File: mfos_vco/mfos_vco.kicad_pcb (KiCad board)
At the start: 2 copper layers, 137.2 x 76.2 mm, 117 parts, among them J1 Conn_01x08_Pin, J2 Conn_01x03_Pin, J3 Conn_01x01_Pin, J4 Conn_01x04_Pin, J5 Conn_01x03_Pin, J6 Conn_01x01_Pin, J7 Conn_01x01_Pin, J8 Conn_01x02_Pin, Q1 PN4391, Q1Ar1 2N3904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

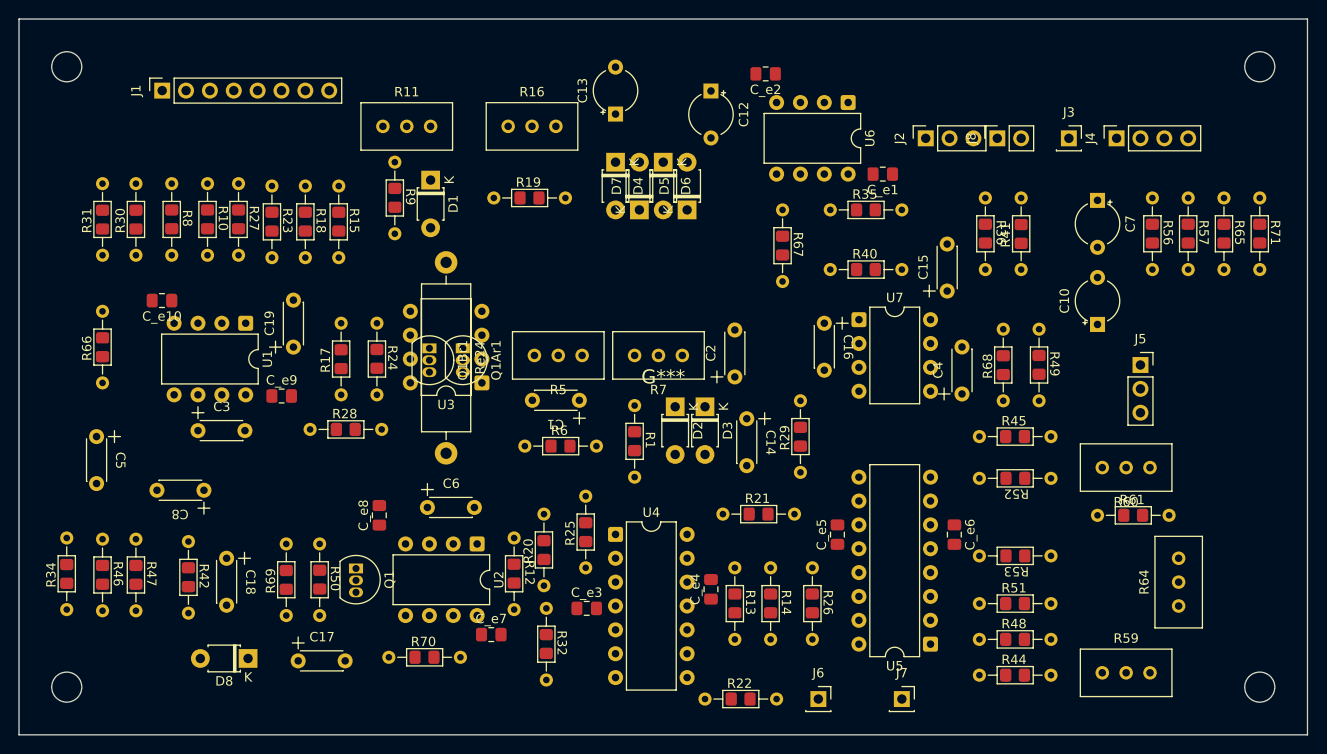
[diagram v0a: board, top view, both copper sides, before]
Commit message: first partial routing
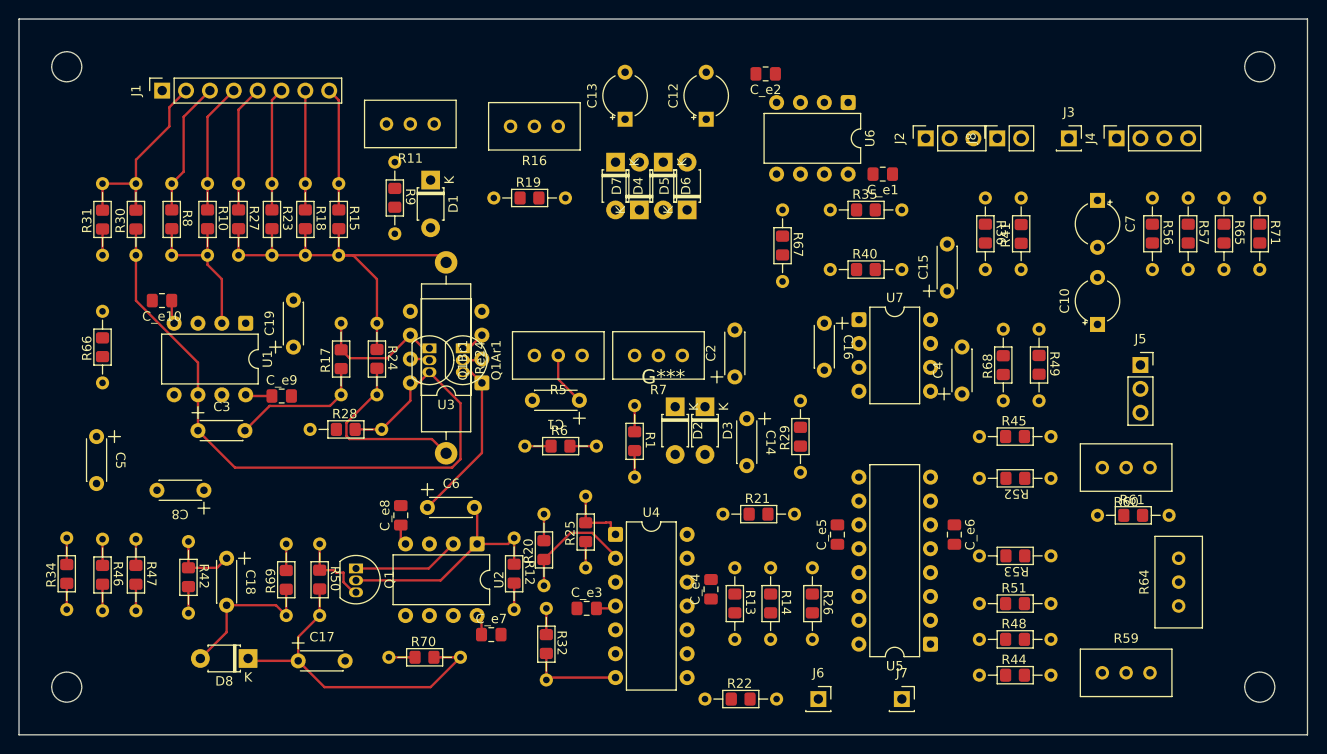
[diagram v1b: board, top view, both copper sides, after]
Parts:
- moved R16 4.83 mm to (166.6, 82.5), turned to 180 degrees
- moved R11 4.71 mm to (153.4, 82.3), turned to 180 degrees
- moved C12 3.05 mm to (187.5, 81.8), turned to 90 degrees
- moved C_e8 2.29 mm to (154.9, 124.0)
- moved C13 1.15 mm to (178.8, 81.8)
- moved R15 0.25 mm to (148.3, 88.6)
- moved R18 0.25 mm to (144.8, 88.6)
- moved R23 0.25 mm to (141.2, 88.6)
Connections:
- C_e9 pad 2: unconnected-(C_e9-Pad2) -> GND
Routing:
- net U1B_c: track 0.00 -> 76.3 mm
- net Net-(U1A--): track 0.00 -> 63.7 mm
- net Net-(D8-K): track 0.00 -> 36.6 mm
- net U1A_c: track 0.00 -> 29.6 mm
- net RAW: track 0.00 -> 28.3 mm
- net LIN: track 0.00 -> 24.1 mm
- net Net-(C19-Pad2): track 0.00 -> 20.1 mm
- net U1_e: track 0.00 -> 16.8 mm
- net Net-(D8-A): track 0.00 -> 16.4 mm
- net Net-(U4A--): track 0.00 -> 15.7 mm
- net +12V: track 0.00 -> 15.7 mm
- net Net-(C3-Pad2): track 0.00 -> 14.6 mm
- net R3P2: track 0.00 -> 14.4 mm
- net R2P2: track 0.00 -> 13.9 mm
- net CV4: track 0.00 -> 13.5 mm
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
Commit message: routing again
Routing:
- net +12V: track 15.7 -> 208.2 mm
- net Net-(C3-Pad2): track 14.6 -> 98.2 mm
- net Net-(C19-Pad2): track 20.1 -> 95.6 mm
- net -12V: track 7.53 -> 78.9 mm
- net Net-(D3-A): track 10.3 -> 54.5 mm
- net Net-(U2B--): track 8.45 -> 51.6 mm
- net Net-(D8-A): track 16.4 -> 53.5 mm
- net Net-(D2-K): track 0.00 -> 20.0 mm
- net Net-(R14-Pad2): track 0.00 -> 19.3 mm
- net Net-(U4B--): track 5.59 -> 24.8 mm
- net Net-(D2-A): track 9.81 -> 28.3 mm
- net U1B_b: track 2.08 -> 17.6 mm
- net RMP: track 0.00 -> 15.0 mm
- net Net-(R5-Pad3): track 2.79 -> 17.1 mm
- net Net-(U4C--): track 0.00 -> 11.3 mm
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
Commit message: FINISHED ROUTING
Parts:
- Q1: footprint Package_TO_SOT_THT:TO-92L_Inline -> Package_TO_SOT_THT:TO-92L_Inline_Wide
- Q1Ar1, Q1Br1: footprint Package_TO_SOT_THT:TO-92_Inline -> Package_TO_SOT_THT:TO-92L_Inline_Wide
- moved D5 3.81 mm to (189.2, 91.4)
- moved D6 3.18 mm to (186.1, 86.4)
- moved D7 2.54 mm to (182.9, 91.4)
- moved D4 1.91 mm to (179.7, 86.4)
- moved Q1Ar1 1.45 mm to (161.9, 104.8)
- moved Q1Br1 1.44 mm to (157.7, 104.8)
- moved D2 1.27 mm to (182.9, 112.4)
- moved D3 0.64 mm to (188.0, 112.4)
- moved R50 0.51 mm to (145.8, 127.0)
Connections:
- R35 pad 2: Net-(R35-Pad2) -> R39P2
- R65 pad 1: R2P2 -> R2P3
- U6 pad 1: Net-(U6A--) -> R39P3
- U6 pad 2: Net-(U6A--) -> R39P3
- U6 pad 6: Net-(U6B--) -> R39P1
- U6 pad 7: Net-(U6B--) -> R39P1
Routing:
- net -12V: track 78.9 -> 554.6 mm, vias 0 -> 2
- net +12V: track 208.2 -> 629.2 mm
- net Net-(R45-Pad1): track 0.00 -> 86.2 mm
- net Net-(R14-Pad2): track 19.3 -> 79.8 mm
- net Net-(D2-K): track 20.0 -> 74.9 mm
- net PWM: track 0.00 -> 51.5 mm
- net Net-(D3-A): track 54.5 -> 100.0 mm
- net Net-(U4A-+): track 5.70 -> 50.5 mm
- net SYNC: track 8.77 -> 52.2 mm
- net Net-(U4C-+): track 9.94 -> 49.8 mm
- net Net-(U7-+): track 0.00 -> 34.0 mm
- net Net-(U5C-+): track 0.00 -> 31.6 mm
- net RAW: track 28.3 -> 59.9 mm
- net Net-(D4-K): track 0.00 -> 30.6 mm
- net GND: track 7.67 -> 34.8 mm, vias 0 -> 27
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- added copper zone on B.Cu, net GND
- added copper zone on F.Cu, net GND
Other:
- board text added: "+12v"
- board text added: "-12v"
- board text added: "CV1"
- board text added: "CV2"
- board text added: "CV3"
- board text added: "CV4"
- board text added: "HFTRIM"
- board text added: "LIN"
- board text added: "PWM"
- board text added: "R2P1"
- board text added: "R2P2"
- board text added: "R2P3"
- board text added: "R39P1"
- board text added: "R39P2"
- board text added: "R39P3"
- board text added: "R3P1"
- board text added: "R3P2"
- board text added: "R3P3"
- board text added: "RMP"
- board text added: "SAWOFST"
- board text added: "SIN"
- board text added: "SINBIAS"
- board text added: "SINLVL"
- board text added: "SINSHAPE"
- board text added: "SQR"
- board text added: "SYNC"
- board text added: "TRI"
- board text added: "TRIOFST"
- board text added: "VOTRIM"
- board text added: "gnd"
